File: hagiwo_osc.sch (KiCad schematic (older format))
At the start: 69 parts, among them J1 VOCT_IN, J10 OUTPUT_PIN, J11 BUTTON_PIN, J2 GAIN_IN, J3 P2_IN, J4 P1_IN, J5 MODECV_IN, J6 Eurorack Power, J7 OUT_A, J8 WIRES_TO_FRONT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

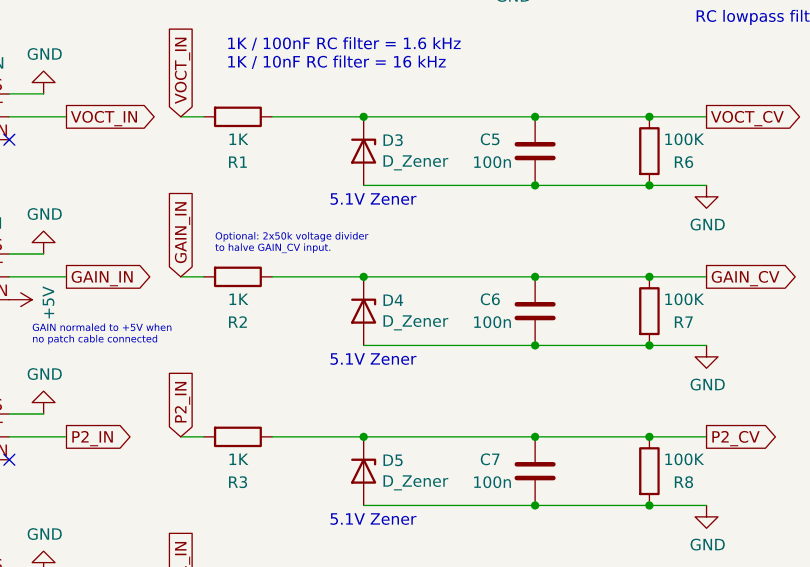
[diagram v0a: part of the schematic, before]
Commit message: Add voltage divider on GAIN_CV since we really need this to prevent clipping.
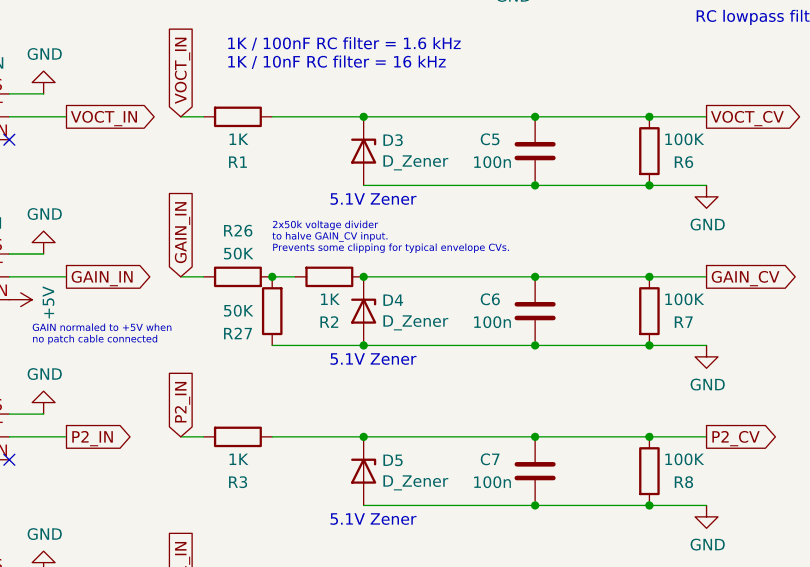
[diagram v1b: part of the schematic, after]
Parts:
- added R26, R27: 50K, Resistor_THT:R_Axial_DIN0204_L3.6mm_D1.6mm_P2.54mm_Vertical, symbol Device:R
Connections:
- net GAIN_IN: now also R26.1; no longer R2.2
- net GND: now also R27.1
- new net: R2.2, R26.2, R27.2
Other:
- note added: "2x50k voltage divider \nto halve GAIN_CV input.\nPrevents some clipping for typical envelope CVs."
- note removed: "Optional: 2x50k voltage divider \nto halve GAIN_CV input."
- moved on the sheet: R2
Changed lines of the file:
@@
 L Device:R R2
 U 1 1 612A06C8
-P 1950 3050
-F 0 "R2" V 2150 3050 50  0000 C CNN
-F 1 "1K" V 2050 3050 50  0000 C CNN
-F 2 "Resistor_THT:R_Axial_DIN0204_L3.6mm_D1.6mm_P2.54mm_Vertical" V 1880 3050 50  0001 C CNN
-F 3 "~" H 1950 3050 50  0001 C CNN
-	1    1950 3050
+P 2350 3050
+F 0 "R2" V 2550 3050 50  0000 C CNN
+F 1 "1K" V 2450 3050 50  0000 C CNN
+F 2 "Resistor_THT:R_Axial_DIN0204_L3.6mm_D1.6mm_P2.54mm_Vertical" V 2280 3050 50  0001 C CNN
+F 3 "~" H 2350 3050 50  0001 C CNN
+	1    2350 3050
 	0    1    1    0
 $EndComp
@@
 	1    0    0    -1
 $EndComp
-Connection ~ 2500 3050
 Wire Wire Line
 	2500 3050 3250 3050
@@
 Text Notes 9400 750  0    31   ~ 0
 Use log pot (A100K) or \noptionally convert to pseudo-log \nusing an extra resistor (10 - 20K between pins 1 and 2)
-Text Notes 1850 2950 0    31   ~ 0
-Optional: 2x50k voltage divider \nto halve GAIN_CV input.
+Text Notes 2100 2950 0    31   ~ 0
+2x50k voltage divider \nto halve GAIN_CV input.\nPrevents some clipping for typical envelope CVs.
 $Comp
 L power:+5V #PWR0104
@@
 GAIN normaled to +5V when\nno patch cable connected
 Wire Wire Line
-	2100 3050 2500 3050
-Wire Wire Line
 	8450 3400 8450 3500
 Wire Wire Line
@@
 Text Notes 2500 950  0    31   ~ 0
 Momentary push button, eg\nPhilips PBS-110 style (or Shin Chin R13-24A)
+$Comp
+L Device:R R26
+U 1 1 61355F7F
+P 1950 3050
+F 0 "R26" V 2150 3050 50  0000 C CNN
+F 1 "50K" V 2050 3050 50  0000 C CNN
+F 2 "Resistor_THT:R_Axial_DIN0204_L3.6mm_D1.6mm_P2.54mm_Vertical" V 1880 3050 50  0001 C CNN
+F 3 "~" H 1950 3050 50  0001 C CNN
+	1    1950 3050
+	0    -1   -1   0
+$EndComp
+$Comp
+L Device:R R27
+U 1 1 613760CD
+P 2100 3200
+F 0 "R27" H 2250 3300 50  0000 C CNN
+F 1 "50K" H 2250 3200 50  0000 C CNN
+F 2 "Resistor_THT:R_Axial_DIN0204_L3.6mm_D1.6mm_P2.54mm_Vertical" V 2030 3200 50  0001 C CNN
+F 3 "~" H 2100 3200 50  0001 C CNN
+	1    2100 3200
+	-1   0    0    1
+$EndComp
+Connection ~ 2500 3050
+Wire Wire Line
+	2100 3350 2500 3350
+Connection ~ 2500 3350
+Wire Wire Line
+	2200 3050 2100 3050
+Connection ~ 2100 3050
 $EndSCHEMATC
